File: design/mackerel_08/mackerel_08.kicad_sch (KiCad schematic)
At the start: 27 parts, among them U1 MC68008FN, U2 SST39SF040, U3 74HC595, U4 GAL16V8, U5 NE555P, X1 CXO_DIP14

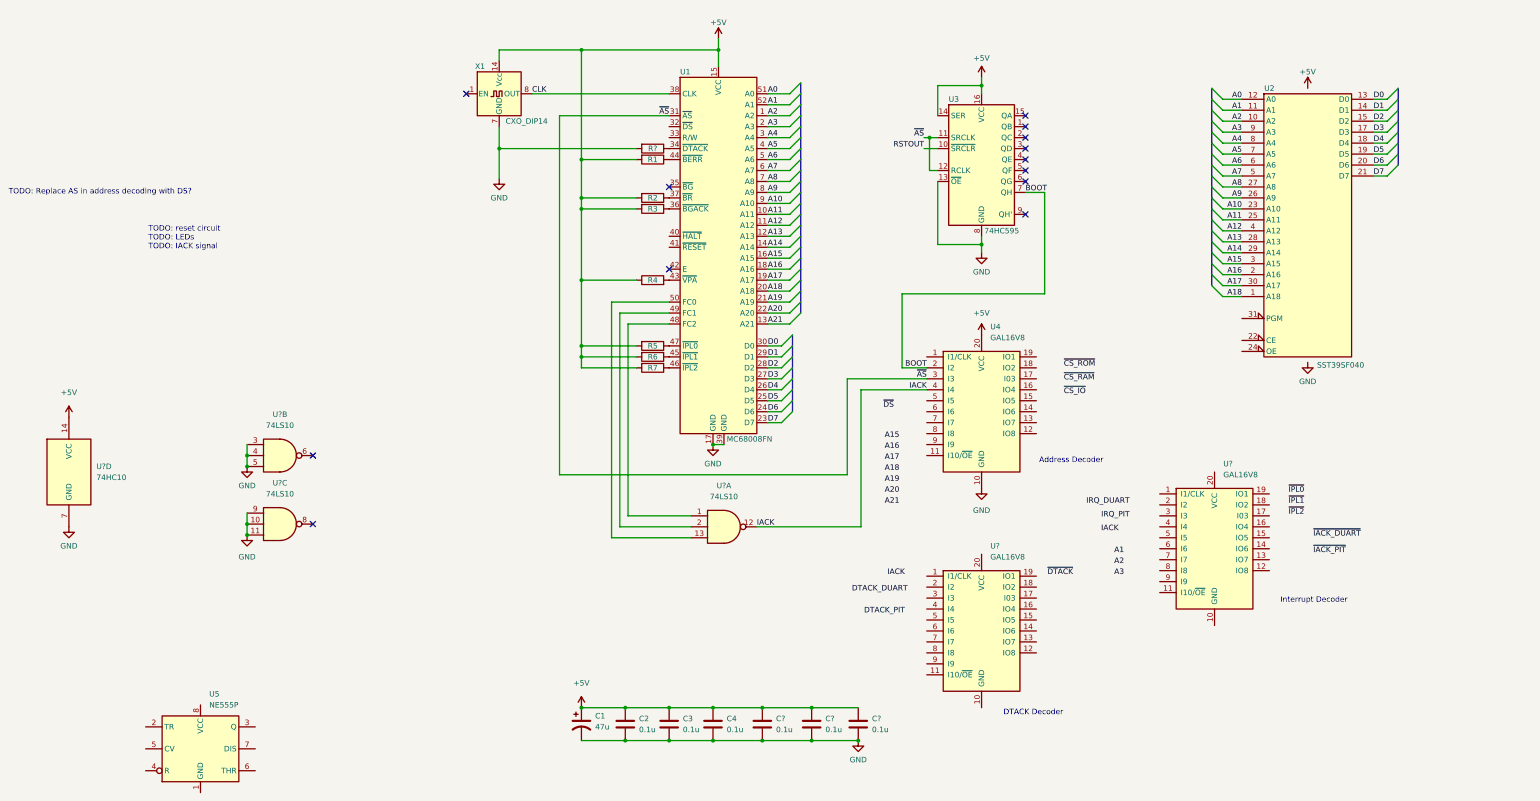
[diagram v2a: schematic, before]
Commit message: Add memory board schematic
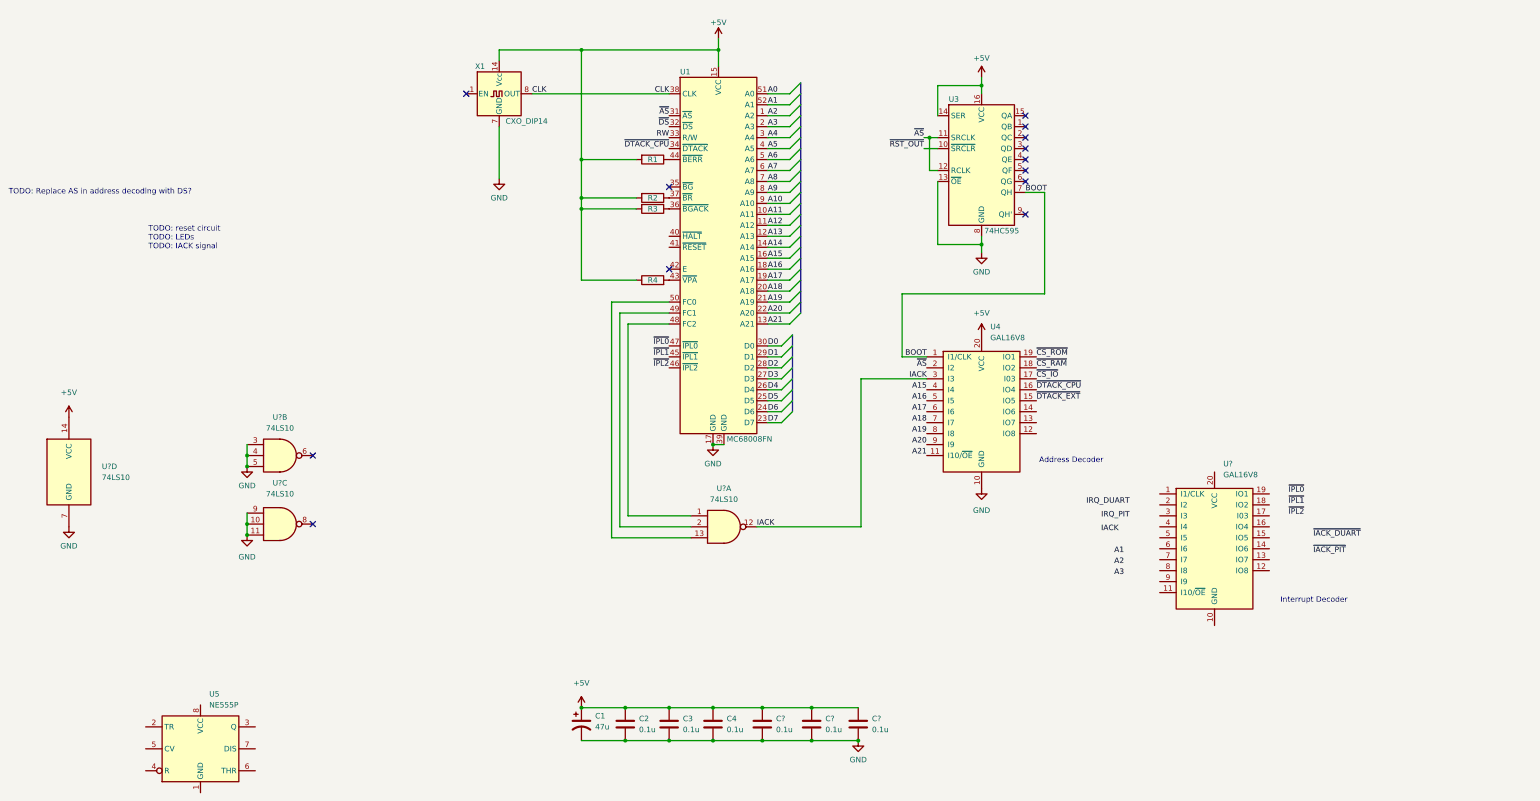
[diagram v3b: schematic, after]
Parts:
- removed R5, R6, R7, R?: 4k7, Resistor_THT:R_Axial_DIN0207_L6.3mm_D2.5mm_P10.16mm_Horizontal, symbol Device:R
- removed U2: SST39SF040, Package_DIP:DIP-32_W15.24mm_Socket, symbol Memory_Flash:SST39SF040
- removed U? (x3): 74LS10, symbol 74xx:74LS10
- removed U?: GAL16V8, Package_DIP:DIP-20_W7.62mm_Socket, symbol Logic_Programmable:GAL16V8
- removed U?: 74HC10, symbol 74xx:74LS10
- added U? (x4): 74LS10, symbol 74xx:74LS10
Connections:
- net +5V: now also U?.14 (VCC)
- net A15: now also U4.4 (I4)
- net A16: now also U4.5 (I5)
- net A17: now also U4.6 (I6)
- net A18: now also U4.7 (I7)
- net A19: now also U4.8 (I8)
- net A20: now also U4.9 (I9)
- net A21: now also U4.11 (I10/~{OE})
- net BOOT: now also U4.1 (I1/CLK); no longer U4.2 (I2)
- net GND: now also U?.10, U?.11, U?.3, U?.4, U?.5, U?.7 (GND), U?.9
- net IACK: now also U4.3 (I3), U?.12; no longer U4.4 (I4)
- net ~{AS}: now also U4.2 (I2); no longer U4.3 (I3)
- net ~{CS_IO}: now also U4.17 (I03)
- net ~{CS_RAM}: now also U4.18 (IO2)
- net ~{CS_ROM}: now also U4.19 (IO1)
- net ~{DS}: now also U1.32 (~{DS})
- net ~{IPL0}: now also U1.47 (~{IPL0})
- net ~{IPL1}: now also U1.45 (~{IPL1})
- net ~{IPL2}: now also U1.46 (~{IPL2})
- net ~{DTACK_CPU}: now reaches U1.34 (~{DTACK})
- net ~{DTACK_CPU}: now also U4.16 (IO4)
- net ~{DTACK_EXT}: now reaches U4.15 (IO5)
- net RW: now reaches U1.33 (R/W)
- net at U1.48 (FC2): now also U?.1
- net at U1.49 (FC1): now also U?.2
- net at U1.50 (FC0): now also U?.13
- net RSTOUT renamed ~{RST_OUT}
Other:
- note removed: "DTACK Decoder"

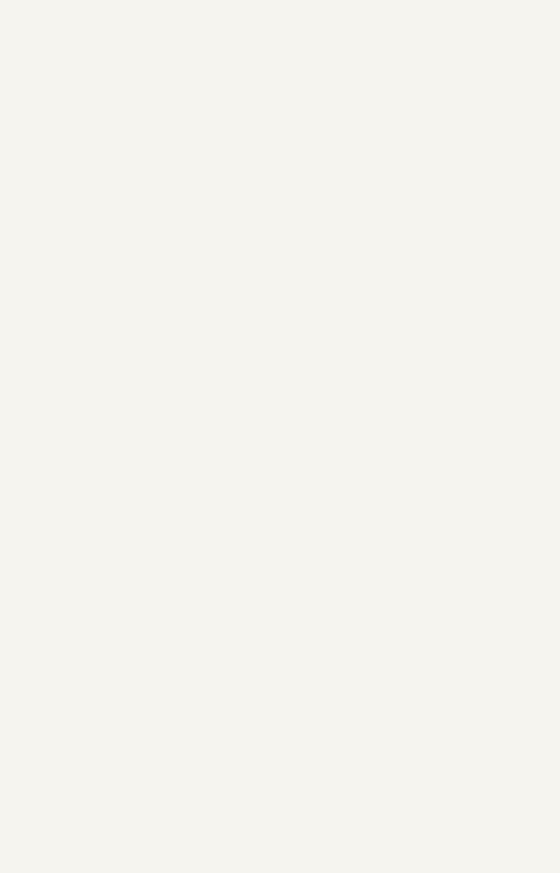
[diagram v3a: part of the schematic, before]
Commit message: Add ROM to schematic
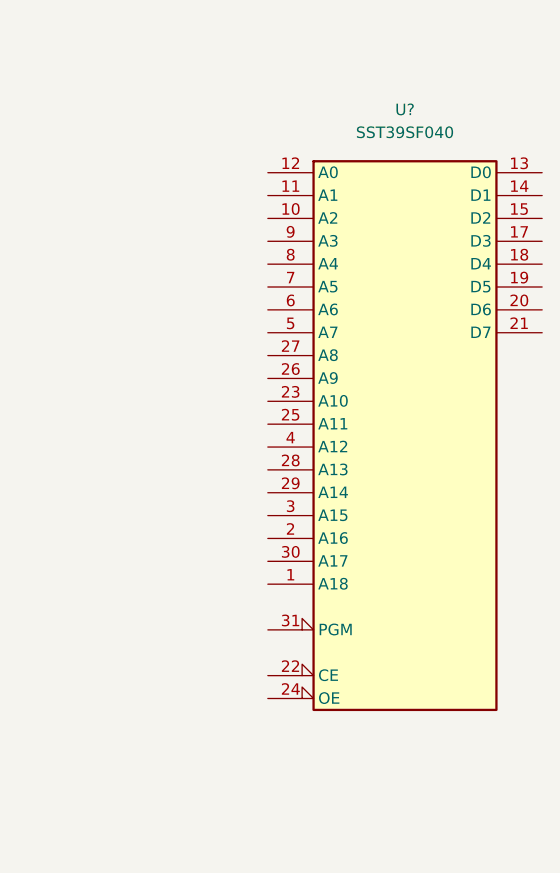
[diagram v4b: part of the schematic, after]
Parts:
- added U?: SST39SF040, symbol Memory_Flash:SST39SF040
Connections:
- net GND: now also U?.16 (GND)
- new net VCC: U?.32 (VCC)
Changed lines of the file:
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@@
+    (pin "9")
+  )
+  (symbol (lib_id "Memory_Flash:SST39SF040") (at 213.995 64.135 0) (unit 1)
+    (in_bom yes) (on_board yes) (fields_autoplaced)
+    (property "Reference" "U?" (id 0) (at 213.995 26.67 0))
+    (property "Value" "SST39SF040" (id 1) (at 213.995 29.21 0))
+    (property "Footprint" "" (id 2) (at 213.995 56.515 0)
+      (effects (font (size 1.27 1.27)) hide)
+    )
+    (property "Datasheet" "http://ww1.microchip.com/downloads/en/DeviceDoc/25022B.pdf" (id 3) (at 213.995 56.515 0)
+      (effects (font (size 1.27 1.27)) hide)
+    )
+    (pin "16")
+    (pin "32")
+    (pin "1")
+    (pin "10")
+    (pin "11")
+    (pin "12")
+    (pin "13")
+    (pin "14")
+    (pin "15")
+    (pin "17")
+    (pin "18")
+    (pin "19")
+    (pin "2")
+    (pin "20")
+    (pin "21")
+    (pin "22")
+    (pin "23")
+    (pin "24")
+    (pin "25")
+    (pin "26")
+    (pin "27")
+    (pin "28")
+    (pin "29")
+    (pin "3")
+    (pin "30")
+    (pin "31")
+    (pin "4")
+    (pin "5")
+    (pin "6")
+    (pin "7")
+    (pin "8")
     (pin "9")
   )
@@
       (reference "U5") (unit 1) (value "NE555P") (footprint "Package_DIP:DIP-8_W7.62mm_Socket")
     )
+    (path "/7f81c500-859e-4579-bf92-5649516ccb03"
+      (reference "U?") (unit 1) (value "SST39SF040") (footprint "")
+    )
     (path "/85fc2c7a-f835-49fb-bc62-2a0db8d97a38"

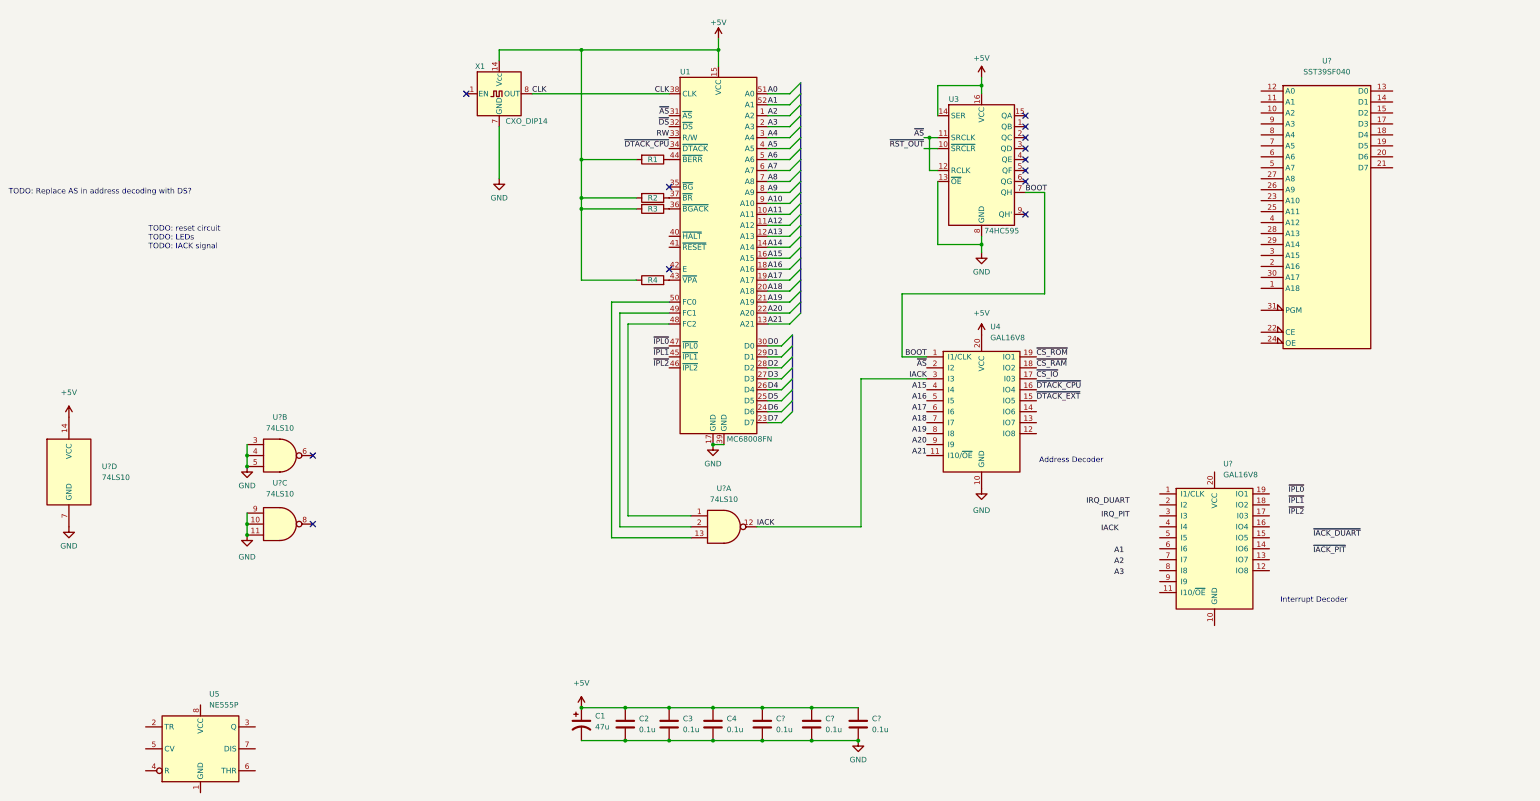
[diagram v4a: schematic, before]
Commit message: Defined system bus pinout and GAL decoding schematic
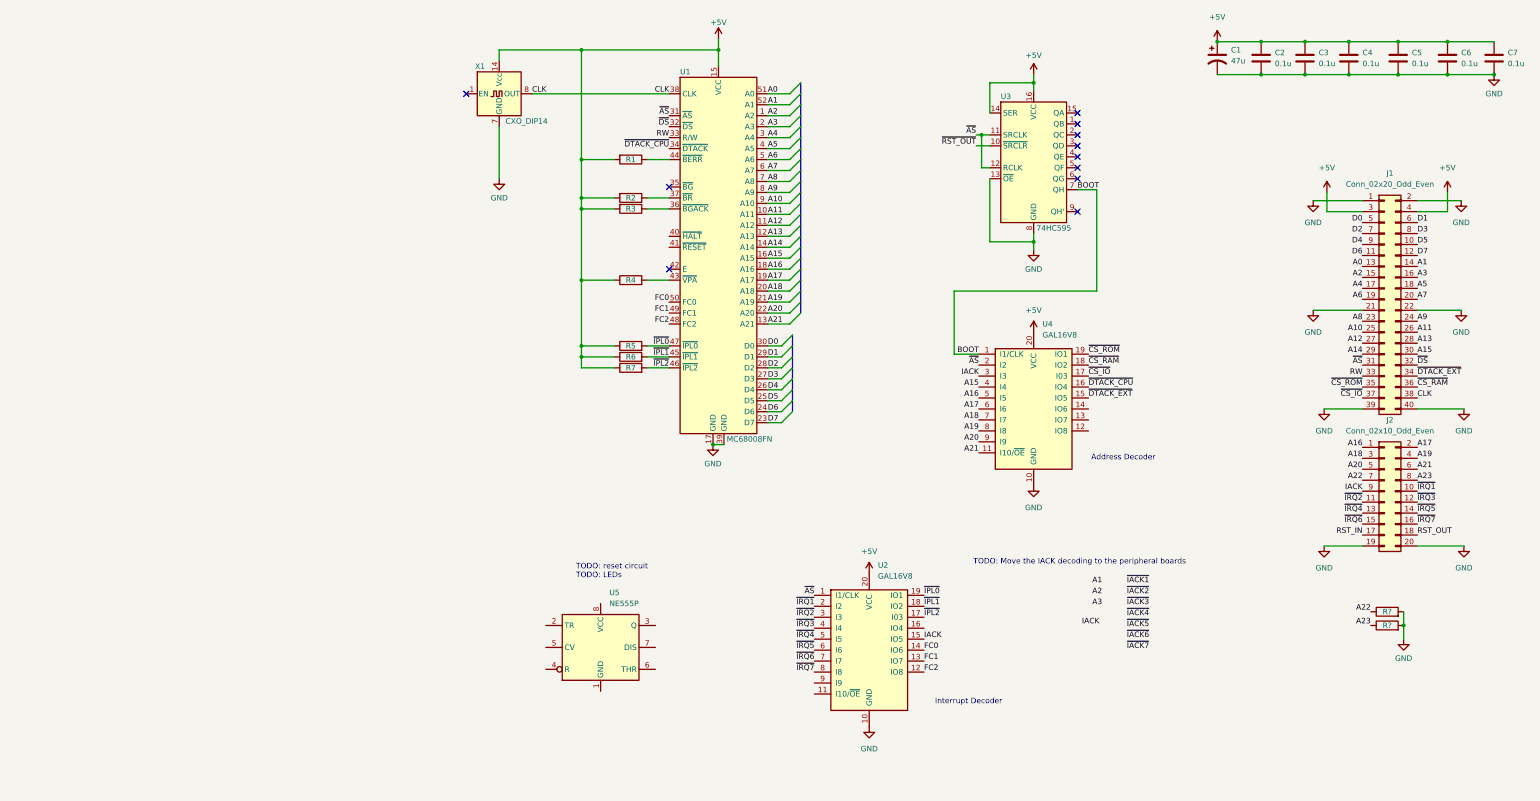
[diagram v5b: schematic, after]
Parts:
- removed U? (x4): 74LS10, symbol 74xx:74LS10
- removed U?: SST39SF040, symbol Memory_Flash:SST39SF040
- added J1: Conn_02x20_Odd_Even, Connector_PinSocket_2.54mm:PinSocket_2x20_P2.54mm_Horizontal, symbol Connector_Generic:Conn_02x20_Odd_Even
- added J2: Conn_02x10_Odd_Even, Connector_PinSocket_2.54mm:PinSocket_2x10_P2.54mm_Horizontal, symbol Connector_Generic:Conn_02x10_Odd_Even
- added R5, R6, R7, R? (x2): 4k7, Resistor_THT:R_Axial_DIN0207_L6.3mm_D2.5mm_P10.16mm_Horizontal, symbol Device:R
- gave numbers to parts that had none: 4
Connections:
- net +5V: now also U2.20 (VCC), J1.3 (Pin_3), J1.4 (Pin_4), R5.1, R6.1, R7.1
- net A0: now also J1.13 (Pin_13)
- net A1: now also J1.14 (Pin_14)
- net A10: now also J1.25 (Pin_25)
- net A11: now also J1.26 (Pin_26)
- net A12: now also J1.27 (Pin_27)
- net A13: now also J1.28 (Pin_28)
- net A14: now also J1.29 (Pin_29)
- net A15: now also J1.30 (Pin_30)
- net A16: now also J2.1 (Pin_1)
- net A17: now also J2.2 (Pin_2)
- net A18: now also J2.3 (Pin_3)
- net A19: now also J2.4 (Pin_4)
- net A2: now also J1.15 (Pin_15)
- net A20: now also J2.5 (Pin_5)
- net A21: now also J2.6 (Pin_6)
- net A3: now also J1.16 (Pin_16)
- net A4: now also J1.17 (Pin_17)
- net A5: now also J1.18 (Pin_18)
- net A6: now also J1.19 (Pin_19)
- net A7: now also J1.20 (Pin_20)
- net A8: now also J1.23 (Pin_23)
- net A9: now also J1.24 (Pin_24)
- net CLK: now also J1.38 (Pin_38)
- net D0: now also J1.5 (Pin_5)
- net D1: now also J1.6 (Pin_6)
- net D2: now also J1.7 (Pin_7)
- net D3: now also J1.8 (Pin_8)
- net D4: now also J1.9 (Pin_9)
- net D5: now also J1.10 (Pin_10)
- net D6: now also J1.11 (Pin_11)
- net D7: now also J1.12 (Pin_12)
- net GND: now also U2.10 (GND), J1.1 (Pin_1), J1.2 (Pin_2), J1.21 (Pin_21), J1.22 (Pin_22), J1.39 (Pin_39), J1.40 (Pin_40), J2.19 (Pin_19), J2.20 (Pin_20), R?.2, R?.2
- net IACK: now also U2.15 (IO5), J2.9 (Pin_9)
- net RW: now also J1.33 (Pin_33)
- net ~{AS}: now also U2.1 (I1/CLK), J1.31 (Pin_31)
- net ~{CS_IO}: now also J1.37 (Pin_37)
- net ~{CS_RAM}: now also J1.36 (Pin_36)
- net ~{CS_ROM}: now also J1.35 (Pin_35)
- net ~{DS}: now also J1.32 (Pin_32)
- net ~{DTACK_EXT}: now also J1.34 (Pin_34)
- net ~{IPL0}: now also U2.19 (IO1), R5.2
- net ~{IPL1}: now also U2.18 (IO2), R6.2
- net ~{IPL2}: now also U2.17 (I03), R7.2
- net FC2: now reaches U1.48 (FC2)
- net FC2: now also U2.12 (IO8)
- net FC1: now reaches U1.49 (FC1)
- net FC1: now also U2.13 (IO7)
- net FC0: now reaches U1.50 (FC0)
- net FC0: now also U2.14 (IO6)
- net ~{IRQ1}: now reaches U2.2 (I2)
- net ~{IRQ1}: now also J2.10 (Pin_10)
- net ~{IRQ2}: now reaches U2.3 (I3)
- net ~{IRQ2}: now also J2.11 (Pin_11)
- net ~{IRQ3}: now reaches U2.4 (I4)
- net ~{IRQ3}: now also J2.12 (Pin_12)
- net ~{IRQ4}: now reaches U2.5 (I5)
- net ~{IRQ4}: now also J2.13 (Pin_13)
- net ~{IRQ5}: now reaches U2.6 (I6)
- net ~{IRQ5}: now also J2.14 (Pin_14)
- net ~{IRQ6}: now reaches U2.7 (I7)
- net ~{IRQ6}: now also J2.15 (Pin_15)
- net ~{IRQ7}: now reaches U2.8 (I8)
- net ~{IRQ7}: now also J2.16 (Pin_16)
- new net A22: J2.7 (Pin_7), R?.1
- new net A23: J2.8 (Pin_8), R?.1
- new net RST_IN: J2.17 (Pin_17)
- new net RST_OUT: J2.18 (Pin_18)
- no-connect marks 13 -> 11
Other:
- note added: "TODO: Move the IACK decoding to the peripheral boards"
- note added: "TODO: reset circuit TODO: LEDs"
- note removed: "TODO: Replace AS in address decoding with DS?"
- note removed: "TODO: reset circuit TODO: LEDs TODO: IACK signal"
- moved on the sheet: C1, C2, C3, C4, C5, C6, C7, R1, R2, R3, R4, U2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
